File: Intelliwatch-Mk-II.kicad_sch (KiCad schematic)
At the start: 33 parts, among them J1 USB_C_Receptacle_USB2.0_16P, SW1 EN Switch, SW2 PROG Swtich, U1 LM7805, U2 CH340C, U3 SN74HC02N, U4 LM1117T-3.3, U5 74AHC1G04GW_125, U6 74AHC1G04GW_125, U7 ESP32-WROOM-32UE

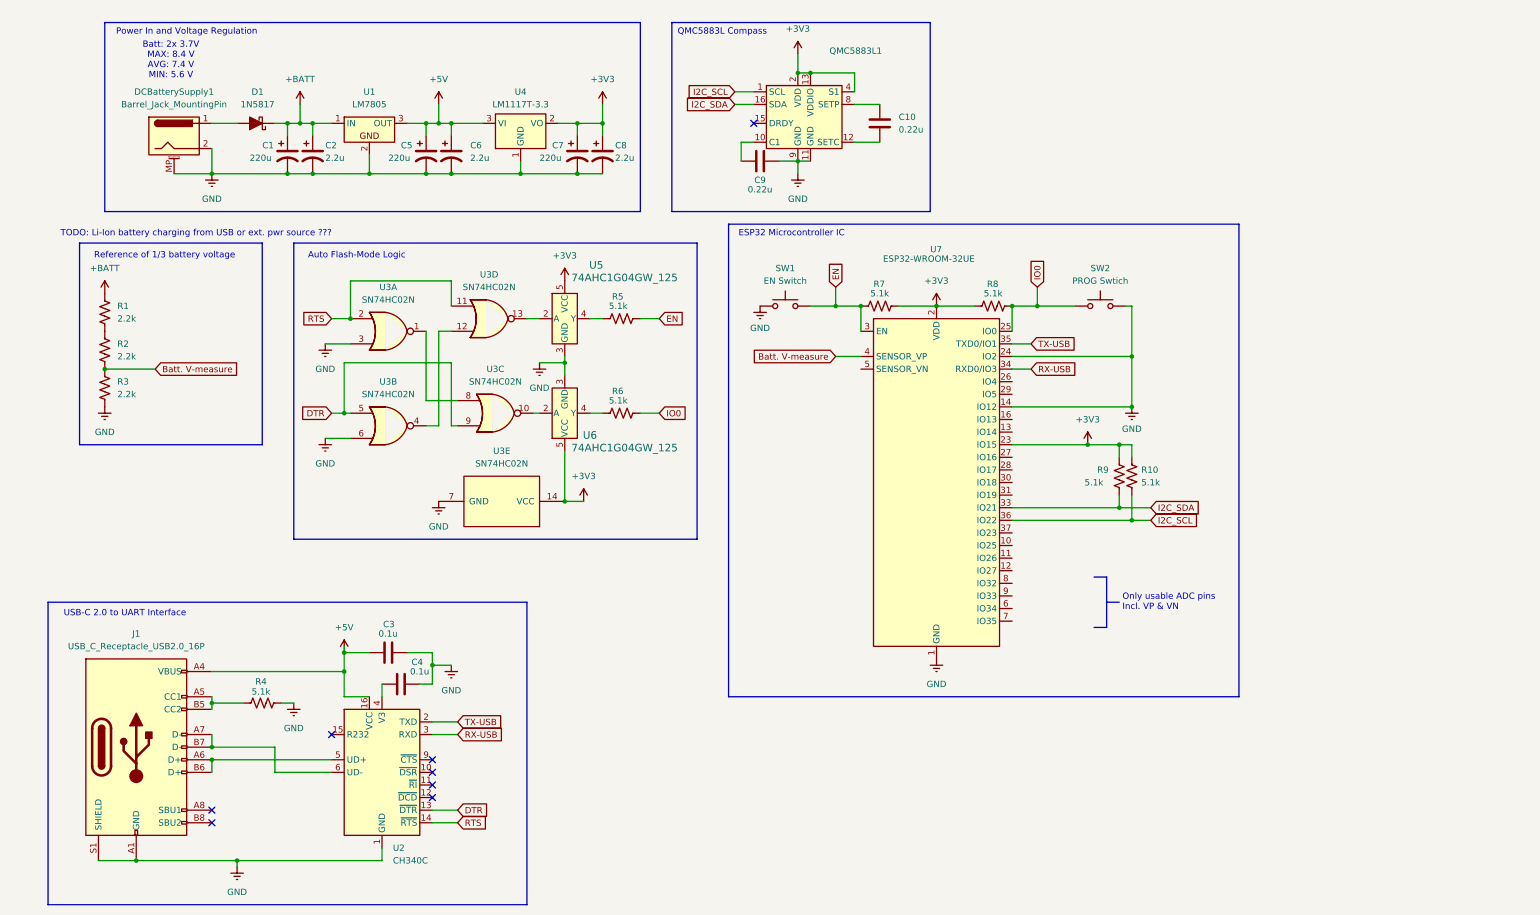
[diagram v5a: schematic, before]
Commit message: ADDED cap to EN pin. ADDED 1.8 TFT SPI LCD with p-MOS on LED pin. TODO connect correct GPIOs to the SPI LCD
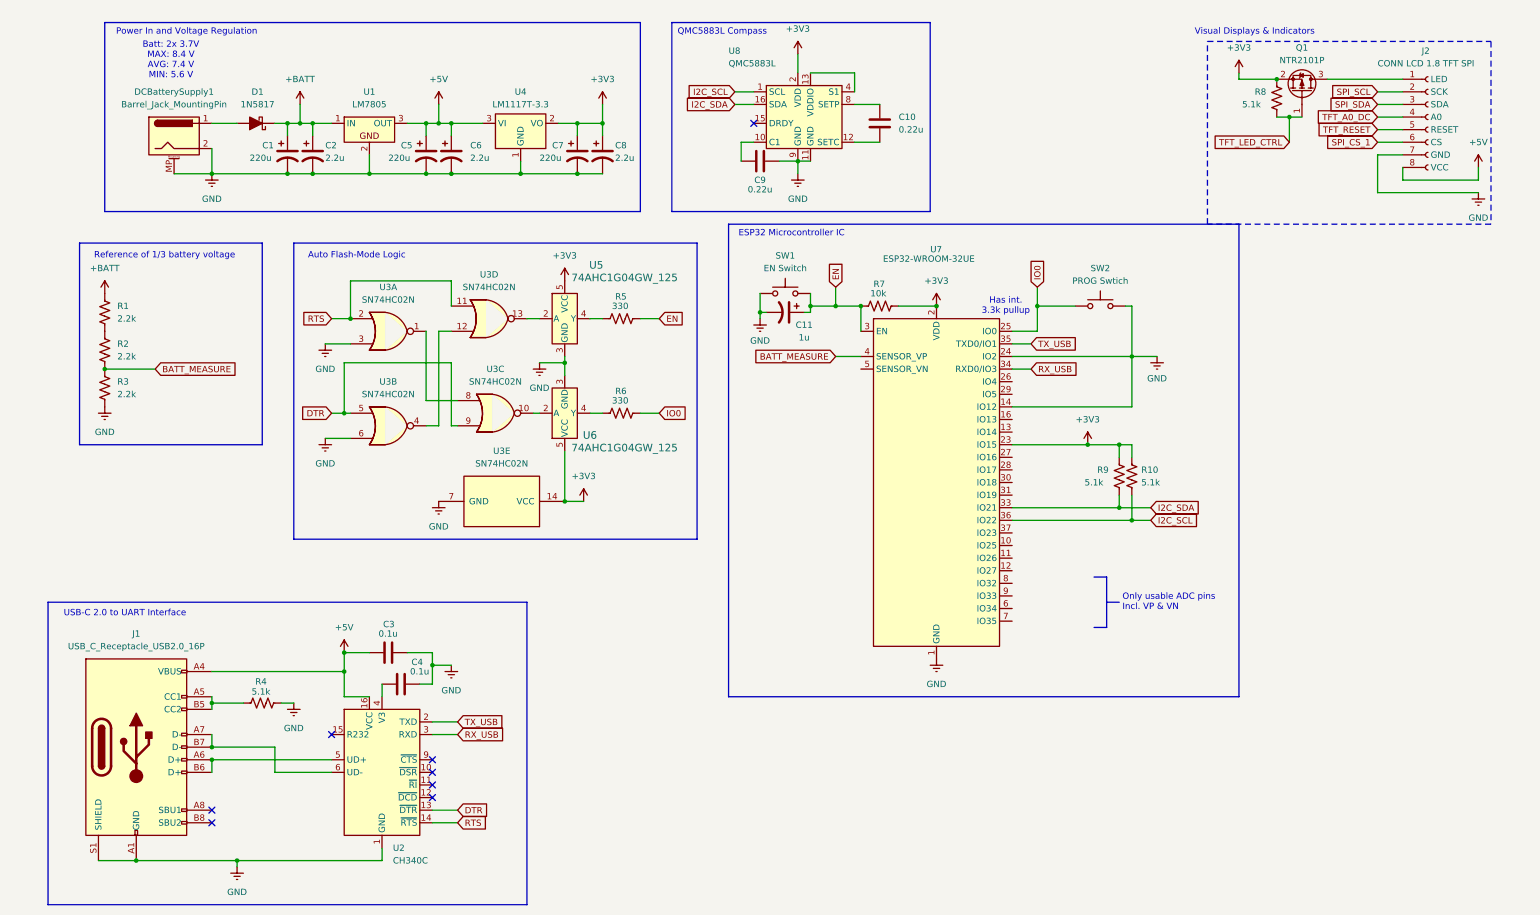
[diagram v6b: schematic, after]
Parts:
- removed QMC5883L1: ~, Package_LGA:LGA-16_3x3mm_P0.5mm, symbol ZCustomSymbols:QMC5883L Compass IC
- added C11: 1u, symbol Device:C_Polarized_US
- added J2: CONN LCD 1.8 TFT SPI, ZCustomFootprints:Conn 1.8 TFT LCD SPI, symbol ZCustomSymbols:CONN LCD 1.8 TFT SPI
- added Q1: NTR2101P, Package_TO_SOT_SMD:SOT-23, symbol Transistor_FET:NTR2101P
- added U8: QMC5883L, Package_LGA:LGA-16_3x3mm_P0.5mm, symbol ZCustomSymbols:QMC5883L Compass IC
- R5, R6: value 5.1k -> 330
- R7: value 5.1k -> 10k
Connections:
- net +3V3: now also R8.1, Q1.2 (S), U8.2 (VDD); no longer R8.2
- net +5V: now also J2.8 (VCC)
- net EN: now also C11.1
- net GND: now also C11.2, J2.7 (GND), U8.11 (GND), U8.9 (GND)
- net I2C_SCL: now also U8.1 (SCL)
- net I2C_SDA: now also U8.16 (SDA)
- net IO0: no longer R8.1
- net at C9.1: now also U8.10 (C1)
- net at C10.2: now also U8.12 (SETC)
- net at C10.1: now also U8.8 (SETP)
- net Batt. V-measure renamed BATT_MEASURE
- net RX-USB renamed RX_USB
- net TX-USB renamed TX_USB
- new net: J2.1 (LED), Q1.3 (D)
- new net: U8.13 (VDDIO), U8.4 (S1)
- new net SPI_CS_1: J2.6 (CS)
- new net SPI_SCL: J2.2 (SCK)
- new net SPI_SDA: J2.3 (SDA)
- new net TFT_A0_DC: J2.4 (A0)
- new net TFT_LED_CTRL: Q1.1 (G), R8.2
- new net TFT_RESET: J2.5 (RESET)
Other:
- note added: "Has int. 3.3k pullup"
- note added: "Visual Displays & Indicators"
- note removed: "TODO: Li-Ion battery charging from USB or ext. pwr source ???"
- moved on the sheet: SW1

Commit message: ADDED connections to both visual displays.
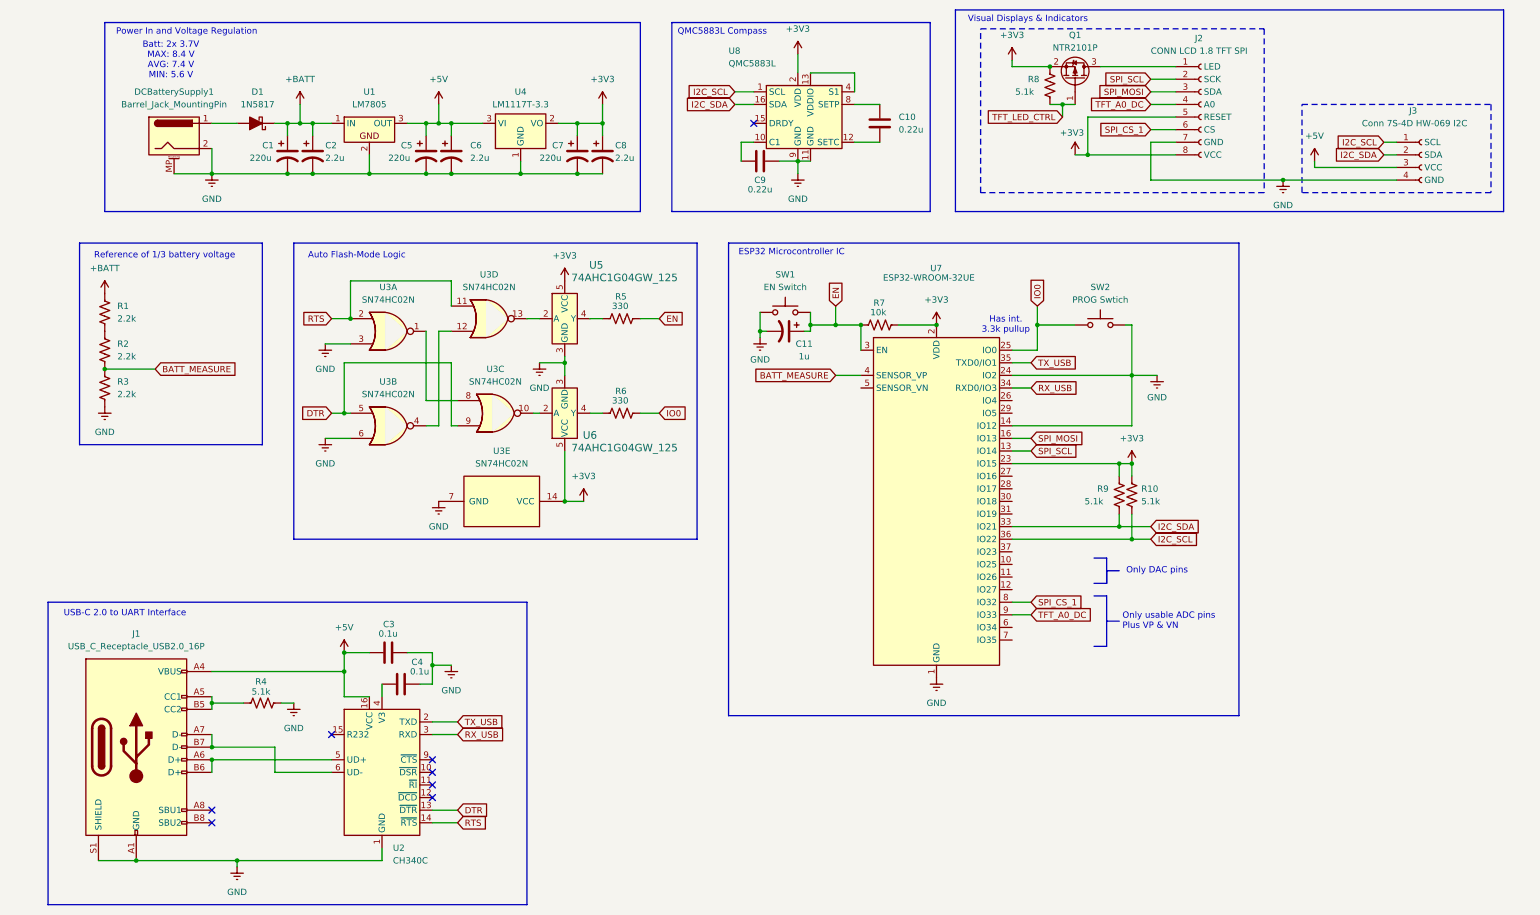
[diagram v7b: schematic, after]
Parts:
- added J3: Conn 7S-4D HW-069 I2C, ZCustomFootprints:Conn 7S-4D HW-069 I2C, symbol ZCustomSymbols:Conn 4-digit 7-seg LEDs I2C HW-069
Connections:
- net SPI_SDA is gone; now on net SPI_MOSI: J2.3 (SDA)
- net TFT_RESET is gone; now on net +3V3: J2.5 (RESET)
- net +3V3: now also J2.8 (VCC)
- net +5V: now also J3.3 (VCC); no longer J2.8 (VCC)
- net GND: now also J3.4 (GND)
- net I2C_SCL: now also J3.1 (SCL)
- net I2C_SDA: now also J3.2 (SDA)
- net SPI_CS_1: now also U7.8 (IO32)
- net SPI_SCL: now also U7.13 (IO14)
- net TFT_A0_DC: now also U7.9 (IO33)
- net SPI_MOSI: now reaches U7.16 (IO13)
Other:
- note added: "Only DAC pins"
- note added: "Only usable ADC pins Plus VP & VN"
- note removed: "Only usable ADC pins Incl. VP & VN"
- moved on the sheet: C11, J2, Q1, R10, R7, R8, R9, SW1, SW2, U7

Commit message: ADDED keyswitches and found 0603 SMD LED to be used for all other indicators in the project. ADDED connections to MOSFETs too. TODO connect keyswitch outputs to ESP32 GPIO pins.
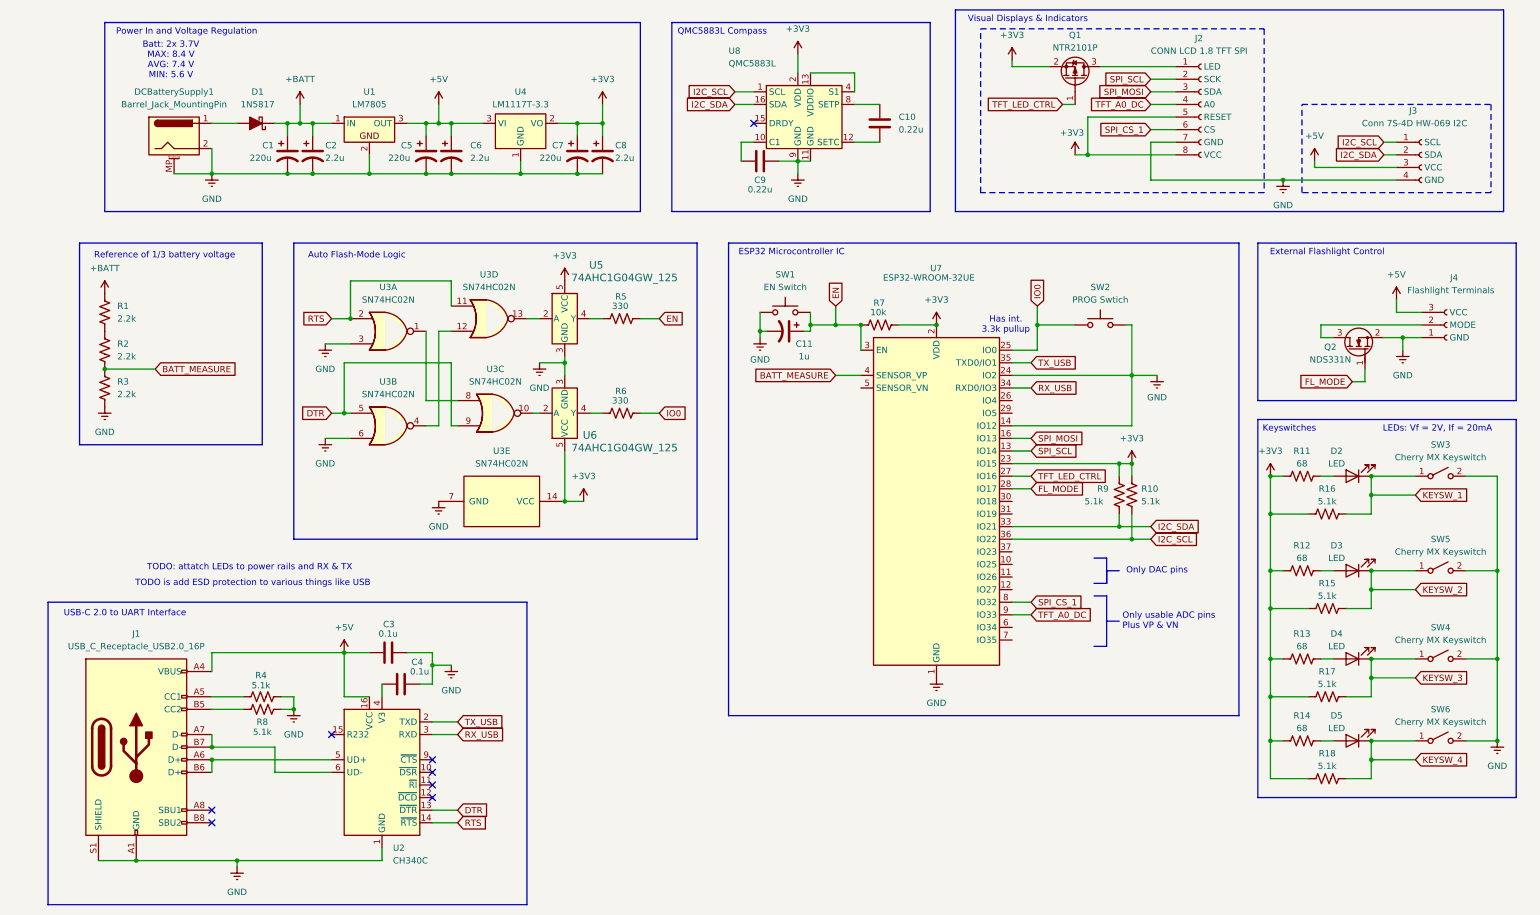
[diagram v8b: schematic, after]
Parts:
- added D2, D3, D4, D5: LED, LED_SMD:LED_0603_1608Metric, symbol Device:LED
- added J4: Flashlight Terminals, Connector_PinSocket_2.54mm:PinSocket_1x03_P2.54mm_Vertical, symbol Connector:Conn_01x03_Socket
- added Q2: NDS331N, PCM_Package_TO_SOT_SMD_AKL:SuperSOT-3, symbol PCM_Transistor_MOSFET_AKL:NDS331N
- added R11, R12, R13, R14: 68, symbol Device:R_US
- added R15, R16, R17, R18: 5.1k, symbol Device:R_US
- added SW3, SW4, SW5, SW6: Cherry MX Keyswitch, Button_Switch_Keyboard:SW_Cherry_MX_1.00u_Plate, symbol Switch:SW_SPST
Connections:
- net +3V3: now also R11.2, R12.2, R13.2, R14.2, R15.2, R16.2, R17.2, R18.2; no longer R8.1
- net +5V: now also J4.3 (VCC)
- net GND: now also R8.2, J4.1 (GND), Q2.2 (S), SW3.2 (B), SW4.2 (B), SW5.2 (B), SW6.2 (B)
- net TFT_LED_CTRL: now also U7.27 (IO16); no longer R8.2
- net at J1.A5 (CC1), R4.1: no longer J1.B5 (CC2)
- net FL_MODE: now reaches U7.28 (IO17)
- net FL_MODE: now also Q2.1 (G)
- new net: D3.2 (A), R12.1
- new net: D5.2 (A), R14.1
- new net: D4.2 (A), R13.1
- new net: D2.2 (A), R11.1
- new net: J1.B5 (CC2), R8.1
- new net: J4.2 (MODE), Q2.3 (D)
- new net KEYSW_1: D2.1 (K), R16.1, SW3.1 (A)
- new net KEYSW_2: D3.1 (K), R15.1, SW5.1 (A)
- new net KEYSW_3: D4.1 (K), R17.1, SW4.1 (A)
- new net KEYSW_4: D5.1 (K), R18.1, SW6.1 (A)
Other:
- note added: "External Flashlight Control"
- note added: "Keyswitches"
- note added: "LEDs: Vf = 2V, If = 20mA"
- note added: "TODO is add ESD protection to various things like USB"
- note added: "TODO: attatch LEDs to power rails and RX & TX"
- moved on the sheet: R4
